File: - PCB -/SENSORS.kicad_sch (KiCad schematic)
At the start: 17 parts, among them U10 QRE1113, U10 VL53L0X, U5 TSOP382xx, U6 QRE1113, U8 QRE1113, U8 VL53L0X, U9 QRE1113, U9 VL53L0X

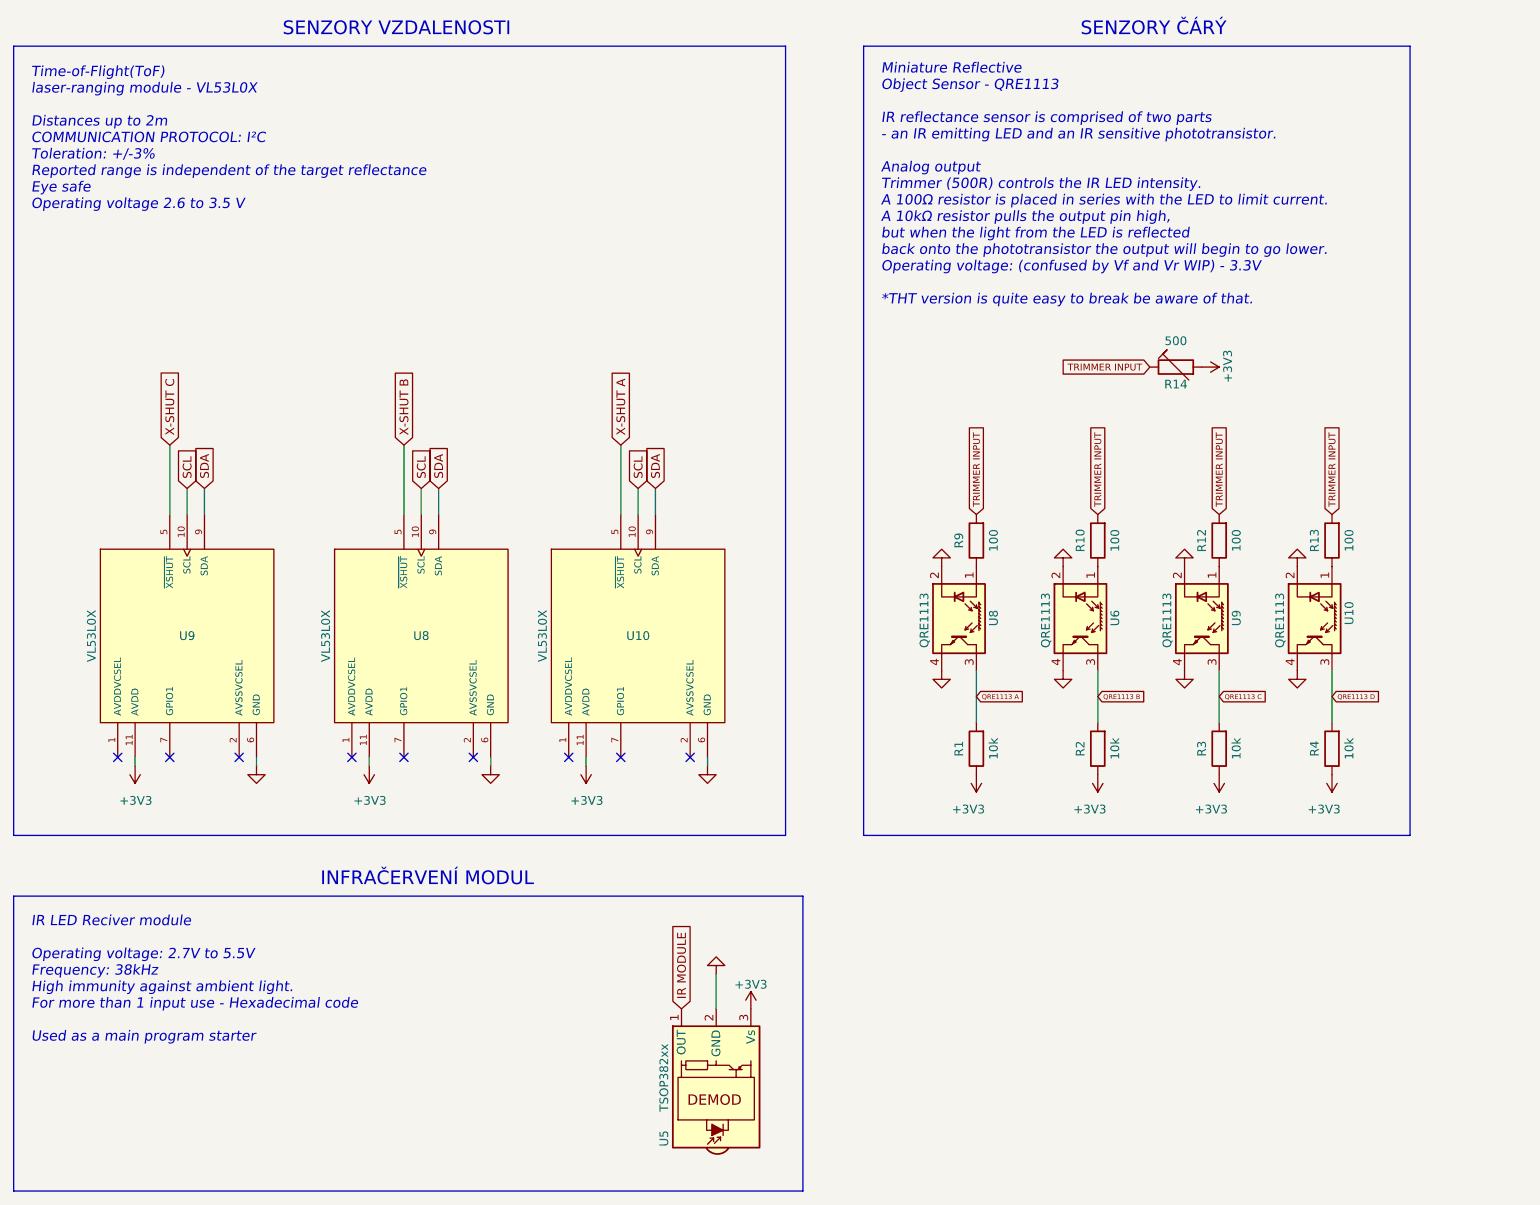
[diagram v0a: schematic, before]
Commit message: PCB - SCH UPDATE (fully labelled and described)
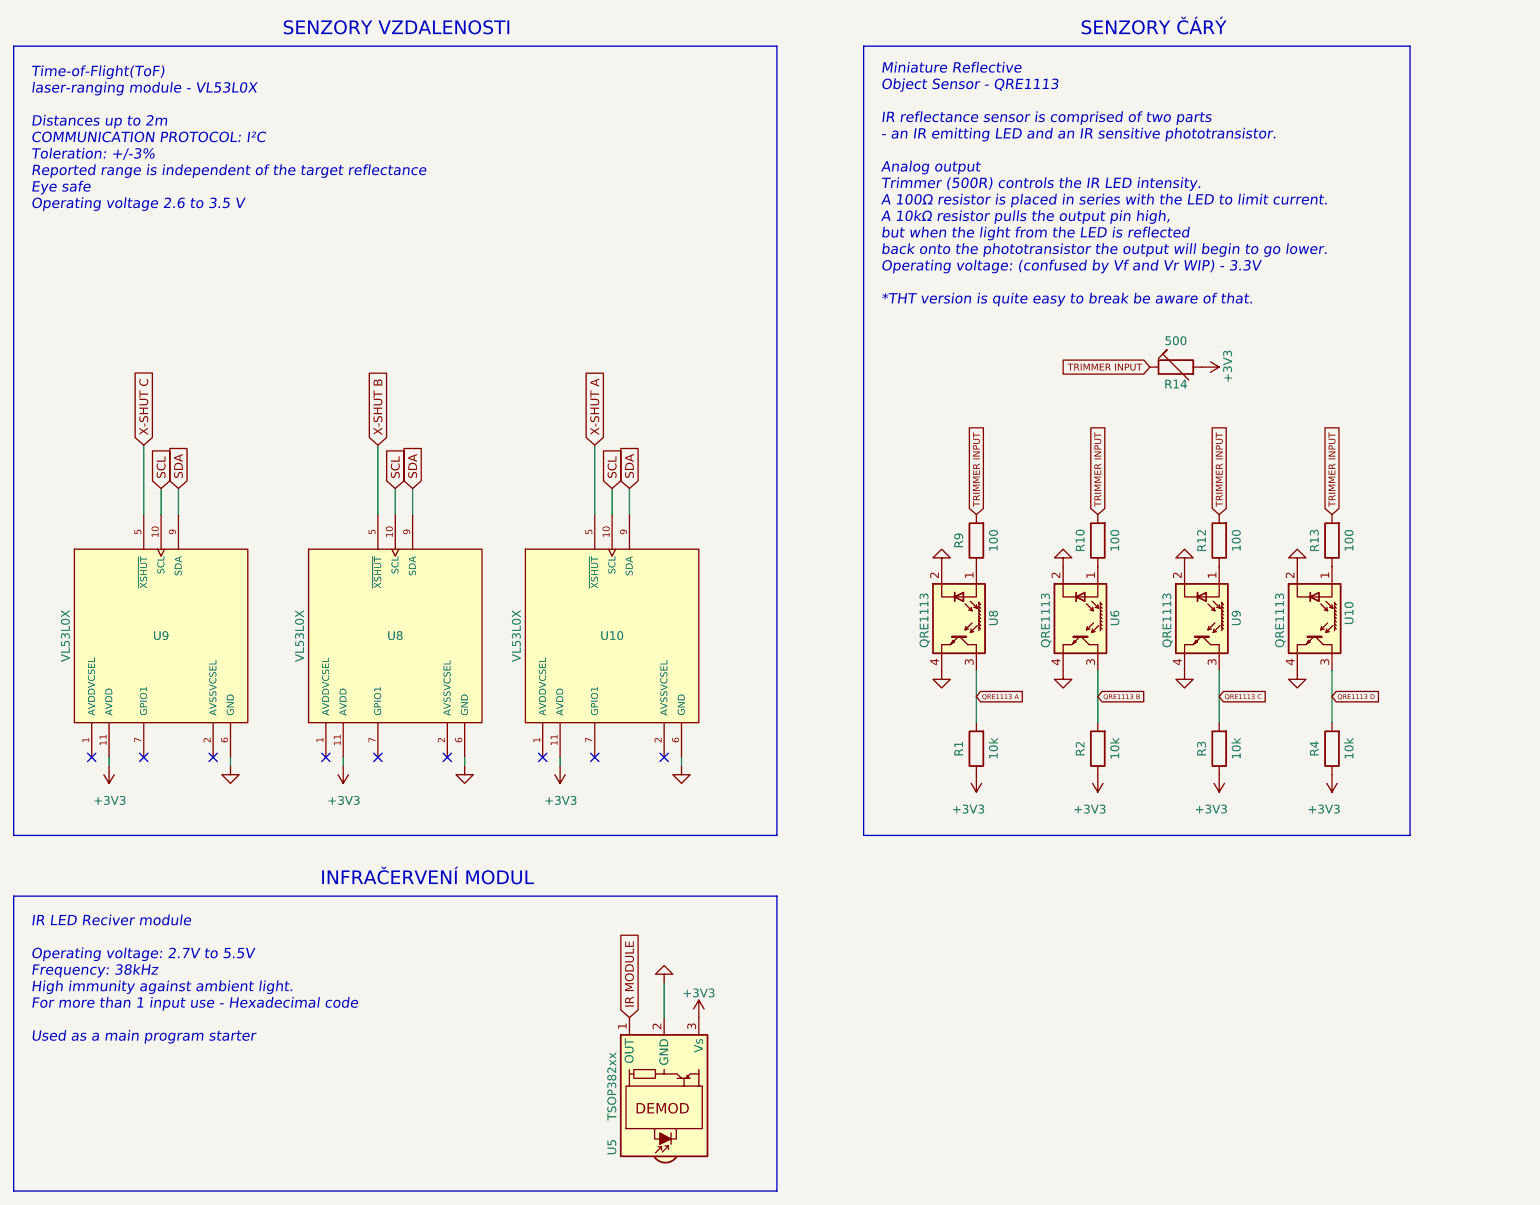
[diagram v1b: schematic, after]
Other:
- moved on the sheet: U10, U5, U8, U9

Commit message: Update SENSORS.kicad_sch
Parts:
- renumbered U8 to U5, U9 to U8, U10 to U9
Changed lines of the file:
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@@
   (symbol (lib_name "GND_1") (lib_id "power:GND") (at 200.66 118.11 0) (unit 1)
     (in_bom yes) (on_board yes) (dnp no) (fields_autoplaced)
-    (property "Reference" "#PWR019" (at 200.66 124.46 0)
+    (property "Reference" "#PWR014" (at 200.66 124.46 0)
       (effects (font (size 1.27 1.27)) hide)
     )
@@
   (symbol (lib_name "GND_1") (lib_id "power:GND") (at 182.88 102.87 180) (unit 1)
     (in_bom yes) (on_board yes) (dnp no) (fields_autoplaced)
-    (property "Reference" "#PWR08" (at 182.88 96.52 0)
+    (property "Reference" "#PWR09" (at 182.88 96.52 0)
       (effects (font (size 1.27 1.27)) hide)
     )
@@
   (symbol (lib_id "Sensor_Proximity:QRE1113") (at 237.49 110.49 270) (unit 1)
     (in_bom yes) (on_board yes) (dnp no)
-    (property "Reference" "U10" (at 242.57 107.95 0)
+    (property "Reference" "U9" (at 242.57 107.95 0)
       (effects (font (size 1.27 1.27)) (justify left))
     )
@@
   (symbol (lib_name "GND_1") (lib_id "power:GND") (at 200.66 102.87 180) (unit 1)
     (in_bom yes) (on_board yes) (dnp no) (fields_autoplaced)
-    (property "Reference" "#PWR011" (at 200.66 96.52 0)
+    (property "Reference" "#PWR013" (at 200.66 96.52 0)
       (effects (font (size 1.27 1.27)) hide)
     )
@@
   (symbol (lib_name "GND_1") (lib_id "power:GND") (at 182.88 118.11 0) (unit 1)
     (in_bom yes) (on_board yes) (dnp no) (fields_autoplaced)
-    (property "Reference" "#PWR07" (at 182.88 124.46 0)
+    (property "Reference" "#PWR011" (at 182.88 124.46 0)
       (effects (font (size 1.27 1.27)) hide)
     )
@@
   (symbol (lib_name "GND_1") (lib_id "power:GND") (at 234.95 102.87 180) (unit 1)
     (in_bom yes) (on_board yes) (dnp no) (fields_autoplaced)
-    (property "Reference" "#PWR018" (at 234.95 96.52 0)
+    (property "Reference" "#PWR023" (at 234.95 96.52 0)
       (effects (font (size 1.27 1.27)) hide)
     )
@@
   (symbol (lib_id "Sensor_Proximity:QRE1113") (at 185.42 110.49 270) (unit 1)
     (in_bom yes) (on_board yes) (dnp no)
-    (property "Reference" "U8" (at 190.5 109.22 0)
+    (property "Reference" "U5" (at 190.5 109.22 0)
       (effects (font (size 1.27 1.27)) (justify left))
     )
@@
   (symbol (lib_id "Sensor_Proximity:QRE1113") (at 220.98 110.49 270) (unit 1)
     (in_bom yes) (on_board yes) (dnp no)
-    (property "Reference" "U9" (at 226.06 109.22 0)
+    (property "Reference" "U8" (at 226.06 109.22 0)
       (effects (font (size 1.27 1.27)) (justify left))
     )
@@
   (symbol (lib_name "GND_1") (lib_id "power:GND") (at 218.44 102.87 180) (unit 1)
     (in_bom yes) (on_board yes) (dnp no) (fields_autoplaced)
-    (property "Reference" "#PWR014" (at 218.44 96.52 0)
+    (property "Reference" "#PWR019" (at 218.44 96.52 0)
       (effects (font (size 1.27 1.27)) hide)
     )
@@
   (symbol (lib_name "GND_1") (lib_id "power:GND") (at 234.95 118.11 0) (unit 1)
     (in_bom yes) (on_board yes) (dnp no) (fields_autoplaced)
-    (property "Reference" "#PWR021" (at 234.95 124.46 0)
-      (effects (font (size 1.27 1.27)) hide)
-    )
+    (property "Reference" "#PWR024" (at 234.95 124.46 0)
+      (effects (font (size 1.27 1.27)) hide)
+    )

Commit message: KiCad project repair
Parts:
- added U11: VL53L0X, symbol sumec_library:GY-530_VL53L0X
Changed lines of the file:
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@@
+    )
+  )
+  (symbol (lib_id "sumec_library:GY-530_VL53L0X") (at 135.89 52.07 0) (unit 1)
+    (in_bom yes) (on_board yes) (dnp no) (fields_autoplaced)
+    (property "Reference" "U11" (at 128.27 41.91 0) (do_not_autoplace)
+      (effects (font (size 1.27 1.27)) (justify left))
+    )
+    (property "Value" "VL53L0X" (at 143.51 62.23 0) (do_not_autoplace)
+      (effects (font (size 1 1)) (justify right))
+    )
+    (property "Footprint" "" (at 123.19 33.02 0)
+      (effects (font (size 1.27 1.27)) hide)
+    )
+    (property "Datasheet" "" (at 123.19 33.02 0)
+      (effects (font (size 1.27 1.27)) hide)
+    )
+    (pin "1")
+    (pin "2")
+    (pin "3")
+    (pin "4")
+    (pin "5")
+    (pin "6")
+    (instances
+      (project "sumec"
+        (path "/fc70a1a8-ed7c-4a0f-9b1a-f23293528385/cfe10bc0-4e7a-493c-9fb6-0f9ed602f83c"
+          (reference "U11") (unit 1)
+        )
+      )
     )
   )

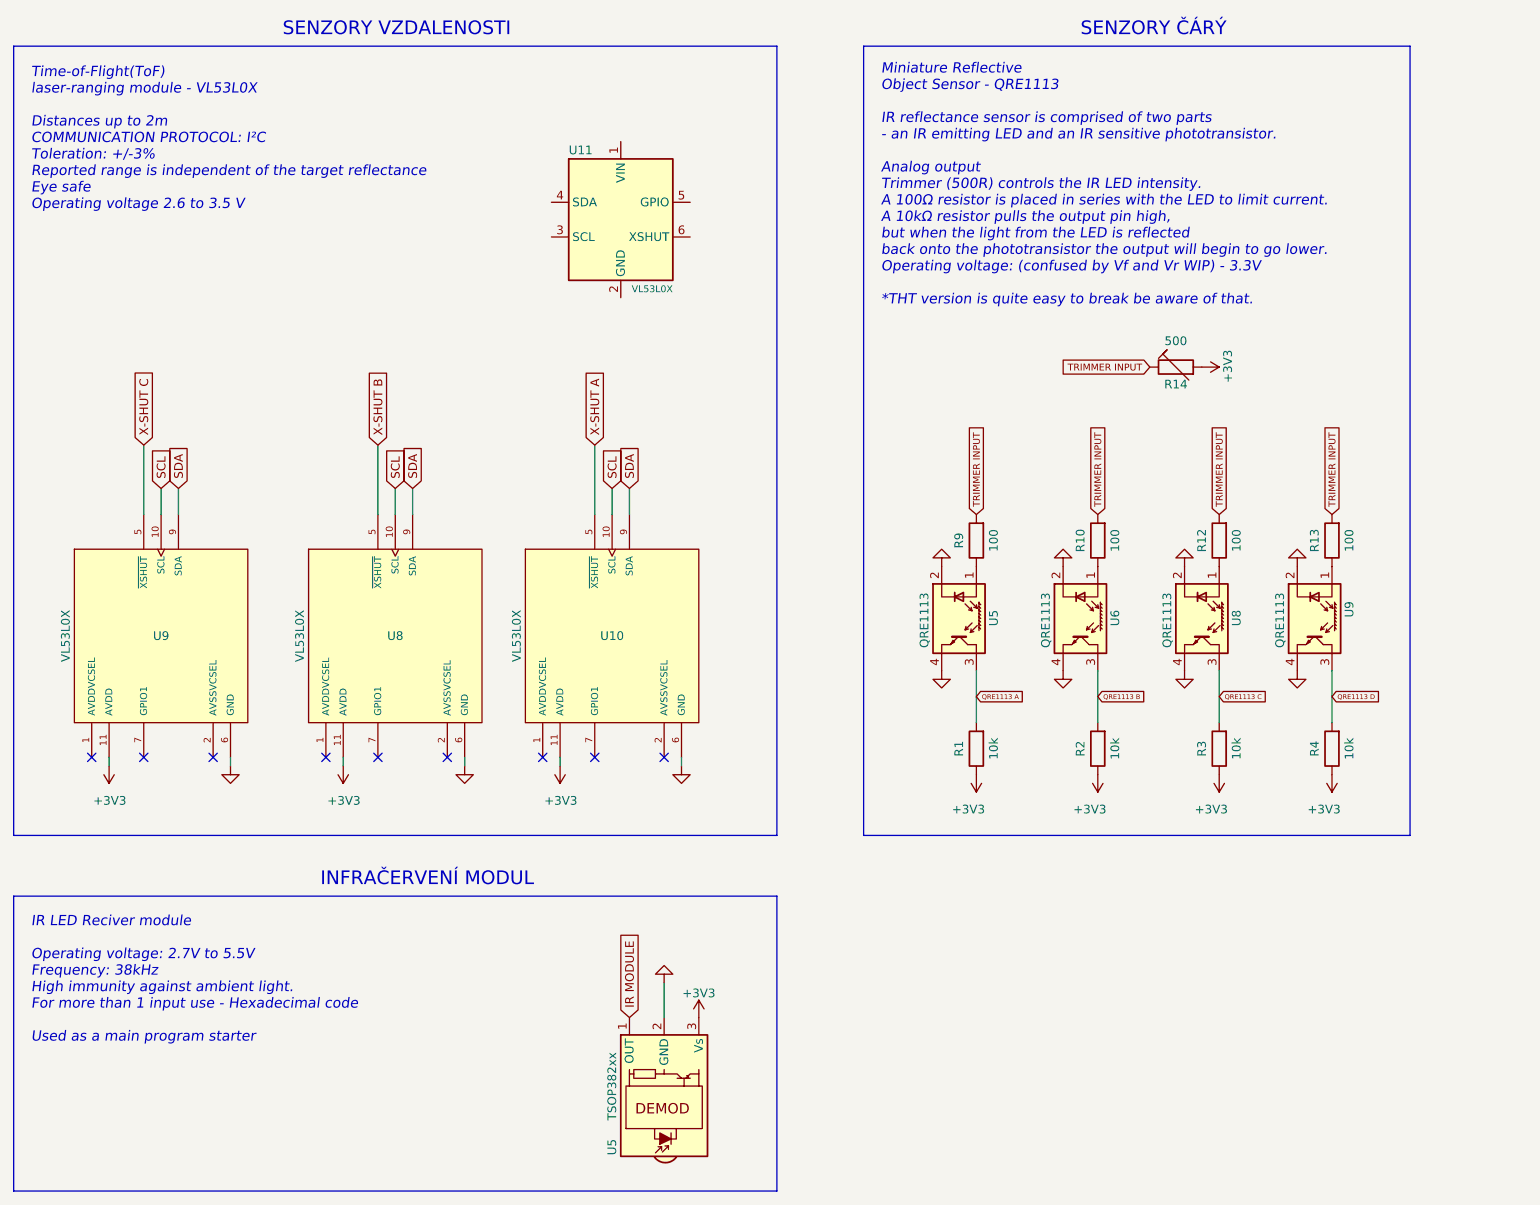
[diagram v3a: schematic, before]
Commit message: PCB - sch and footprint update, QRE1113 3D model.
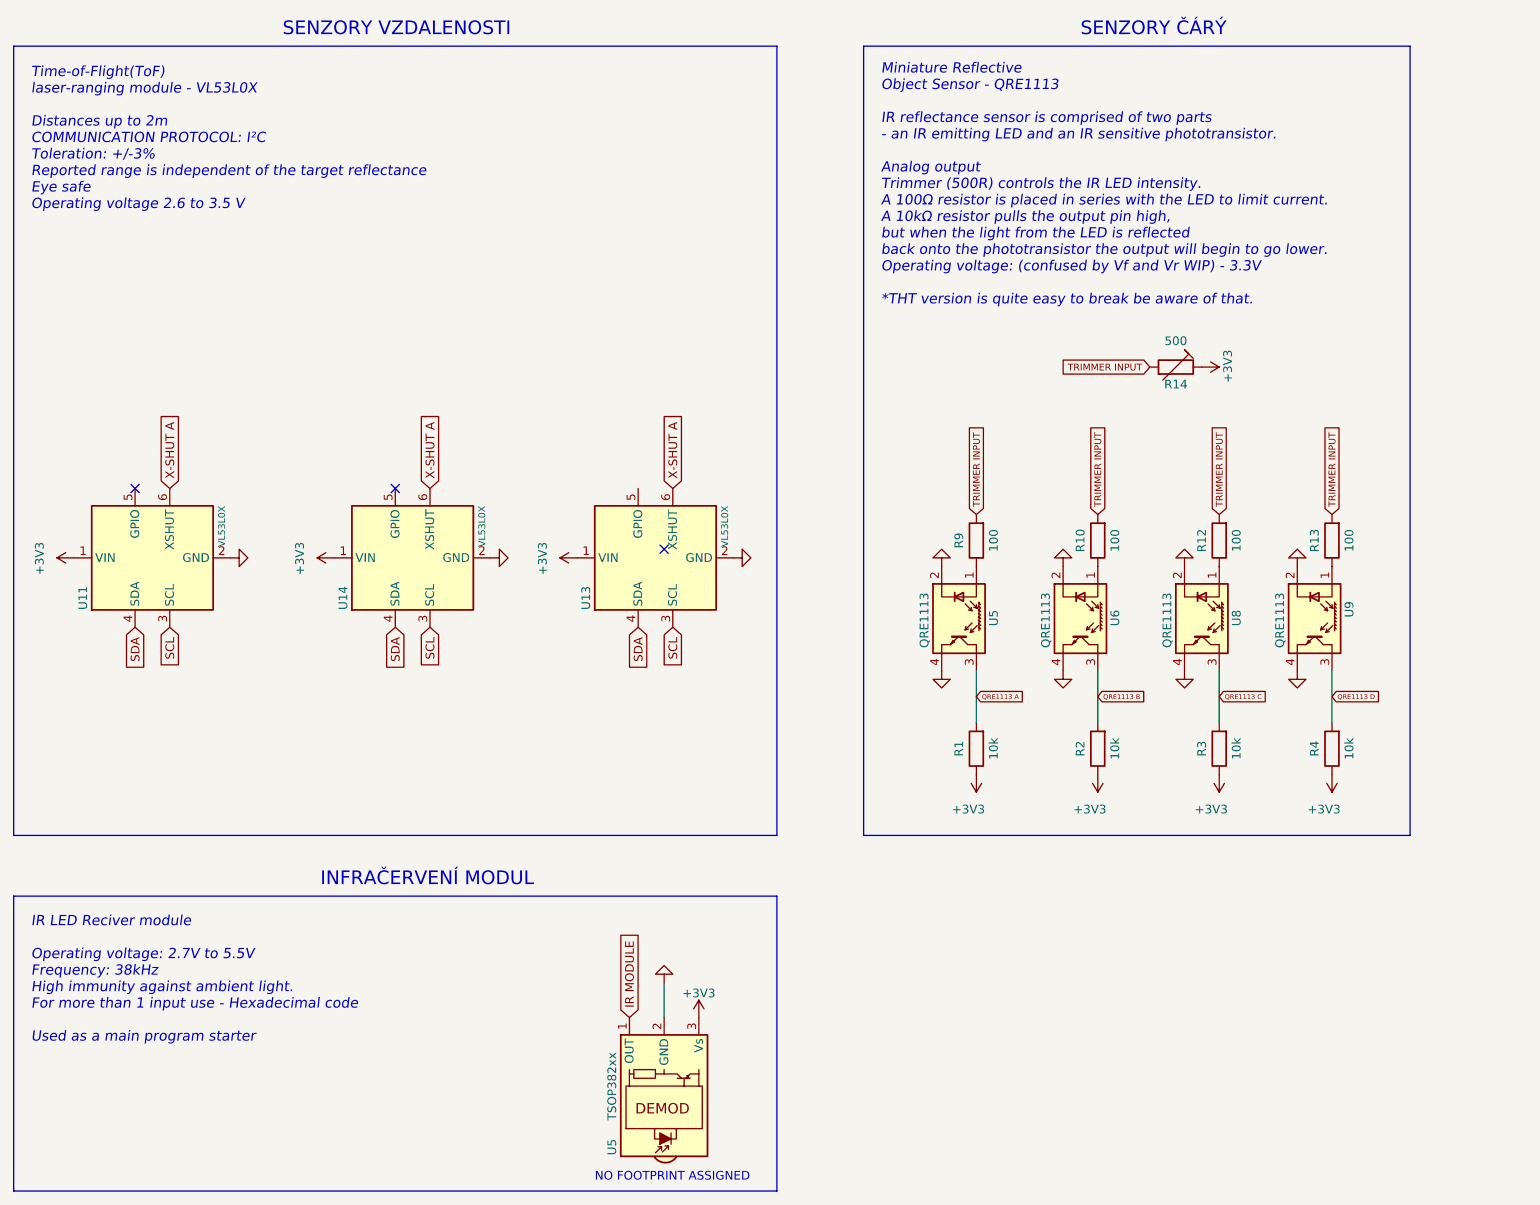
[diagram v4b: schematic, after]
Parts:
- removed U10, U8, U9: VL53L0X, SENSOR_VL53L0X, symbol VL53L0X:VL53L0X
- added U13, U14: VL53L0X, sumec_library:GY-530 VL53L0X, symbol sumec_library:GY-530_VL53L0X
- U11: footprint (none) -> sumec_library:GY-530 VL53L0X
- U5: footprint OptoDevice:Vishay_MINICAST-3Pin -> (none)
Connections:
- net +3V3: now also R14.1, U11.1 (VIN), U13.1 (VIN), U14.1 (VIN); no longer R14.2
- net GND: now also U11.2 (GND), U13.2 (GND), U14.2 (GND)
- net SCL: now also U11.3 (SCL), U13.3 (SCL), U14.3 (SCL)
- net SDA: now also U11.4 (SDA), U13.4 (SDA), U14.4 (SDA)
- net TRIMMER INPUT: now also R14.2; no longer R14.1
- net X-SHUT A: now also U11.6 (XSHUT), U13.6 (XSHUT), U14.6 (XSHUT)
- no-connect marks 9 -> 3
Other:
- note added: "NO FOOTPRINT ASSIGNED"
- moved on the sheet: R14, U11

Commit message: PCB - Board update
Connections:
- net GPIO: now reaches U13.5 (GPIO)
- net GPIO: now also U11.5 (GPIO), U14.5 (GPIO)
- no-connect marks 3 -> 0
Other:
- note added: "*potrebujeme GPIO?"
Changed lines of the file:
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@@
 (kicad_sch (version 20230121) (generator eeschema)
   (paper "A4")
-  (no_connect (at 102.87 91.44))
-  (no_connect (at 142.24 100.33))
-  (no_connect (at 64.77 91.44))
   (wire (pts (xy 187.96 118.11) (xy 187.96 125.73))
     (stroke (width 0) (type default))
@@
     (effects (font (size 1.5 1.5) italic) (justify left bottom))
   )
+  (text "*potrebujeme GPIO?" (at 90.17 74.93 0)
+    (effects (font (size 2 2)) (justify left bottom))
+  )
   (text "IR LED Reciver module\n\nOperating voltage: 2.7V to 5.5V\nFrequency: 38kHz \nHigh immunity against ambient light. \nFor more than 1 input use - Hexadecimal code\n\nUsed as a main program starter\n"
     (at 49.53 172.72 0)
@@
     )
   )
+  (global_label "GPIO" (shape input) (at 64.77 91.44 90) (fields_autoplaced)
+    (effects (font (size 1.27 1.27)) (justify left))
+    (property "Intersheetrefs" "${INTERSHEET_REFS}" (at 64.77 84.0589 90)
+      (effects (font (size 1.27 1.27)) (justify left) hide)
+    )
+  )
   (global_label "X-SHUT A" (shape input) (at 69.85 91.44 90) (fields_autoplaced)
     (effects (font (size 1.27 1.27)) (justify left))
@@
     )
   )
+  (global_label "GPIO" (shape input) (at 138.43 91.44 90) (fields_autoplaced)
+    (effects (font (size 1.27 1.27)) (justify left))
+    (property "Intersheetrefs" "${INTERSHEET_REFS}" (at 138.43 84.0589 90)
+      (effects (font (size 1.27 1.27)) (justify left) hide)
+    )
+  )
+  (global_label "GPIO" (shape input) (at 102.87 91.44 90) (fields_autoplaced)
+    (effects (font (size 1.27 1.27)) (justify left))
+    (property "Intersheetrefs" "${INTERSHEET_REFS}" (at 102.87 84.0589 90)
+      (effects (font (size 1.27 1.27)) (justify left) hide)
+    )
+  )
